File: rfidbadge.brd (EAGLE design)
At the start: 93.7 x 48.2 mm, 49 parts, among them Q1 BSS123, U1 ATMEGA328P_TQFP, U2 CLRC663, Y1 27.12 MHz

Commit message: Lots of layout
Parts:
- C10: device rcl:085CS_1AR -> SparkFun-Passives:EIA7343
- C28: value (none) -> 0.1 uF
- L1, L2, L3: device rcl:L0201 -> SparkFun-Passives:0603
- moved C26 16.8 mm to (54.9, 37.1)
- moved C28 15.5 mm to (52.1, 33.0), turned to 270 degrees
- moved R6 7.53 mm to (58.1, 37.1), turned to 180 degrees
- moved C16 6.67 mm to (35.6, 25.7)
- moved R4 6.24 mm to (60.0, 31.4)
- moved C27 5.83 mm to (55.6, 25.4), turned to 180 degrees
- moved C23 5.43 mm to (56.5, 27.9), turned to 270 degrees
- moved C5 5.41 mm to (48.6, 26.4), turned to 270 degrees
- moved R3 5.26 mm to (52.4, 27.6)
- moved R2 4.97 mm to (52.4, 29.8)
- moved Q1 4.93 mm to (36.8, 39.7), turned to 90 degrees
- moved C10 4.80 mm to (47.3, 45.1)
- moved R1 3.86 mm to (33.7, 40.6), turned to 90 degrees
- moved C21 2.69 mm to (56.5, 31.1), turned to 270 degrees
- moved L3 2.31 mm to (54.3, 32.4), turned to 180 degrees
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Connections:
- net GND: now also C10.C; no longer C10.-
- net VDD: now also C10.A; no longer C10.+
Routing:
- net GND: track 0.00 -> 23.2 mm
- net N$9: track 0.00 -> 15.0 mm
- net RXP: track 0.00 -> 10.9 mm, vias 0 -> 2
- net VDD: track 0.00 -> 10.7 mm
- net XTAL1: track 0.00 -> 7.74 mm
- net VMID: track 0.00 -> 7.73 mm
- net XTAL2: track 0.00 -> 7.31 mm
- net TVDD: track 0.00 -> 7.28 mm
- net N$1: track 0.00 -> 6.17 mm
- net N$2: track 0.00 -> 5.74 mm
- net TX1: track 0.00 -> 5.42 mm
- net C2-: track 0.00 -> 5.11 mm
- net C1-: track 0.00 -> 5.09 mm
- net N$6: track 0.00 -> 4.91 mm
- net TX2: track 0.00 -> 4.21 mm
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
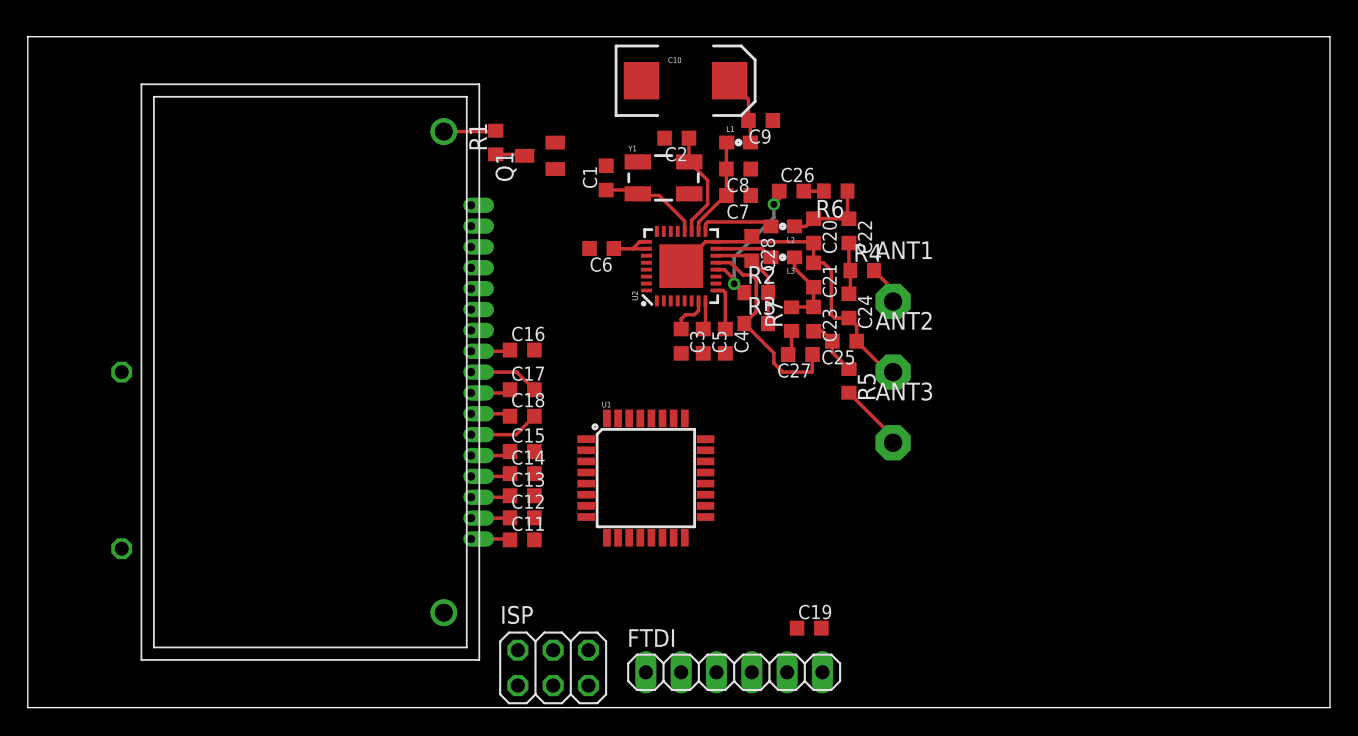
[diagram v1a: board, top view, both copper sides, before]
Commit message: Add antenna trace and ground planes
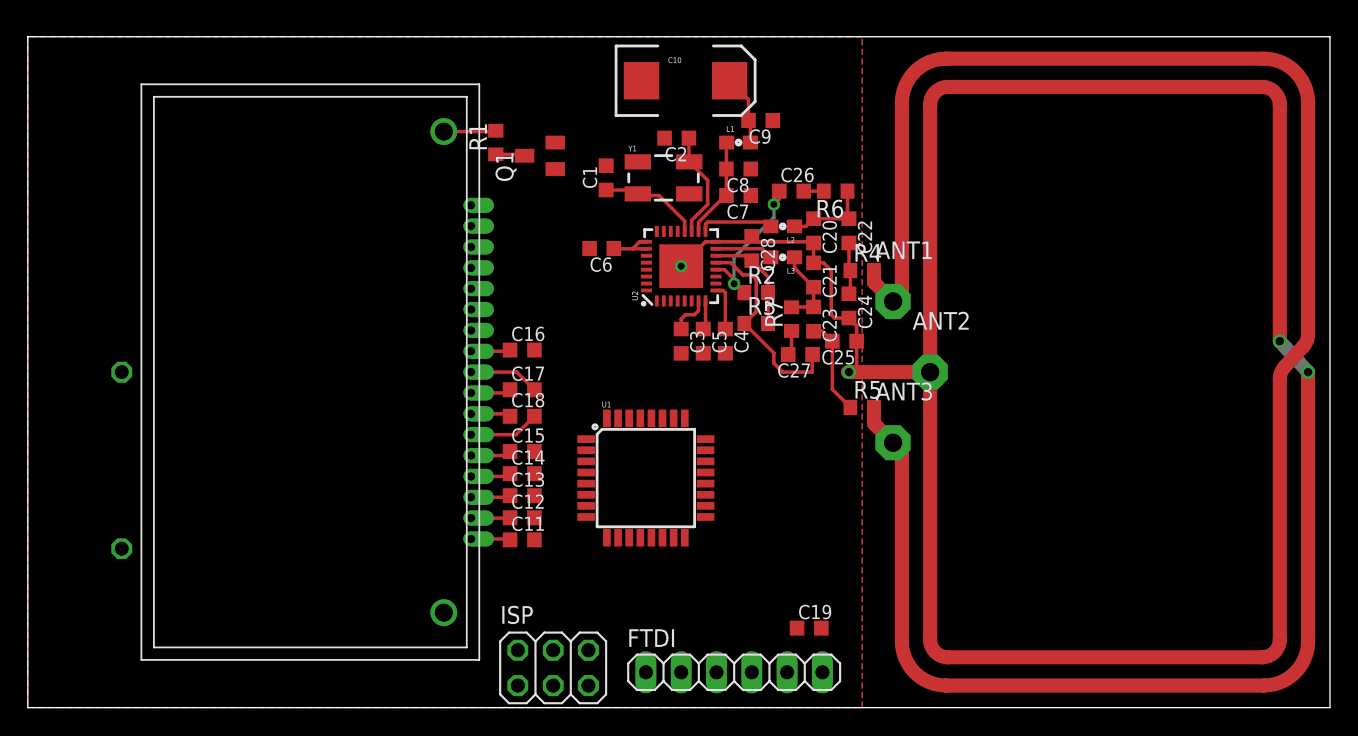
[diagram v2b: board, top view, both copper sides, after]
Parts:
- moved ANT2 2.67 mm to (64.9, 24.1)
- moved R5 2.13 mm to (60.0, 21.6), turned to 0 degrees
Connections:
- removed net N$5: ANT1.1, R4.2
- removed net N$6: ANT3.1, R5.2
- net GND: now also ANT1.1, ANT3.1, R4.2, R5.2
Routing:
- net GND: track 23.2 -> 297.3 mm, vias 0 -> 4
- net N$6: track 4.91 -> 0.00 mm
- net N$4: track 4.14 -> 6.94 mm
- net N$5: track 2.79 -> 0.00 mm
- added copper zone on layer 1, net GND
- added copper zone on layer 16, net GND
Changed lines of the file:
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@@
 <setting verticaltext="up"/>
 </settings>
-<grid distance="0.0125" unitdist="inch" unit="inch" style="lines" multiple="1" display="no" altdistance="0.025" altunitdist="inch" altunit="inch"/>
+<grid distance="0.0125" unitdist="inch" unit="inch" style="lines" multiple="1" display="yes" altdistance="0.025" altunitdist="inch" altunit="inch"/>
 <layers>
 <layer number="1" name="Top" color="4" fill="1" visible="yes" active="yes"/>
@@
 </element>
 <element name="R4" library="rcl" package="R0603" value="" x="60.0075" y="31.4325"/>
-<element name="R5" library="rcl" package="R0603" value="" x="59.055" y="23.495" rot="R270"/>
+<element name="R5" library="rcl" package="R0603" value="" x="60.0075" y="21.59"/>
 <element name="ANT1" library="discrete" package="PAD-01" value="" x="62.23" y="29.21"/>
-<element name="ANT2" library="discrete" package="PAD-01" value="" x="62.23" y="24.13"/>
+<element name="ANT2" library="discrete" package="PAD-01" value="" x="64.897" y="24.13"/>
 <element name="ANT3" library="discrete" package="PAD-01" value="" x="62.23" y="19.05"/>
 <element name="R6" library="rcl" package="R0603" value="" x="58.1025" y="37.1475" rot="R180"/>
@@
 <contactref element="FTDI" pad="2"/>
 <contactref element="U$1" pad="NEG"/>
-<wire x1="49.49" y1="33.5" x2="48.74" y2="33.5" width="0.254" layer="1"/>
-<wire x1="48.74" y1="33.5" x2="46.99" y2="31.75" width="0.254" layer="1"/>
 <wire x1="49.49" y1="33.5" x2="56.43" y2="33.5" width="0.254" layer="1"/>
 <wire x1="56.43" y1="33.5" x2="56.515" y2="33.415" width="0.254" layer="1"/>
@@
 <wire x1="59.6125" y1="26.3525" x2="59.6125" y2="27.46" width="0.254" layer="1"/>
 <wire x1="59.6125" y1="27.46" x2="59.055" y2="28.0175" width="0.254" layer="1"/>
-<wire x1="59.6125" y1="26.3525" x2="61.835" y2="24.13" width="0.254" layer="1"/>
-<wire x1="61.835" y1="24.13" x2="62.23" y2="24.13" width="0.254" layer="1"/>
-<wire x1="51.9925" y1="38.735" x2="53.58" y2="42.2275" width="0" layer="19" extent="1-1"/>
-<wire x1="51.9925" y1="36.83" x2="51.9925" y2="38.735" width="0" layer="19" extent="1-1"/>
-<wire x1="52.07" y1="33.895" x2="51.9925" y2="36.83" width="0" layer="19" extent="1-1"/>
-<wire x1="49.49" y1="33.5" x2="52.07" y2="33.895" width="0" layer="19" extent="1-1"/>
-<wire x1="46.99" y1="25.4775" x2="46.99" y2="31.75" width="0" layer="19" extent="1-1"/>
-<wire x1="48.5775" y1="25.4775" x2="46.99" y2="25.4775" width="0" layer="19" extent="1-1"/>
-<wire x1="50.165" y1="25.4775" x2="48.5775" y2="25.4775" width="0" layer="19" extent="1-1"/>
-<wire x1="45.7975" y1="40.9575" x2="51.9925" y2="38.735" width="0" layer="19" extent="1-1"/>
-<wire x1="44.1375" y1="45.085" x2="45.7975" y2="40.9575" width="0" layer="19" extent="1-1"/>
-<wire x1="41.5925" y1="38.975" x2="45.7975" y2="40.9575" width="0" layer="19" extent="1-1"/>
-<wire x1="37.93" y1="40.6375" x2="41.5925" y2="38.975" width="0" layer="19" extent="1-1"/>
-<wire x1="40.4" y1="33.02" x2="41.5925" y2="38.975" width="0" layer="19" extent="1-1"/>
-<wire x1="36.435" y1="25.7175" x2="40.4" y2="33.02" width="0" layer="19" extent="1-1"/>
-<wire x1="31.87" y1="27.13" x2="36.435" y2="25.7175" width="0" layer="19" extent="1-1"/>
-<wire x1="36.435" y1="18.415" x2="36.435" y2="25.7175" width="0" layer="19" extent="1-1"/>
-<wire x1="36.435" y1="16.8275" x2="36.435" y2="18.415" width="0" layer="19" extent="1-1"/>
-<wire x1="36.435" y1="15.24" x2="36.435" y2="16.8275" width="0" layer="19" extent="1-1"/>
-<wire x1="36.435" y1="13.6525" x2="36.435" y2="15.24" width="0" layer="19" extent="1-1"/>
-<wire x1="36.435" y1="12.065" x2="36.435" y2="13.6525" width="0" layer="19" extent="1-1"/>
-<wire x1="40.1574" y1="17.71" x2="36.435" y2="18.415" width="0" layer="19" extent="1-1"/>
-<wire x1="40.1574" y1="16.11" x2="40.1574" y2="17.71" width="0" layer="19" extent="1-1"/>
-<wire x1="48.7426" y1="16.91" x2="48.5775" y2="25.4775" width="0" layer="19" extent="1-1"/>
-<wire x1="40.3225" y1="4.1275" x2="36.435" y2="12.065" width="0" layer="19" extent="1-1"/>
-<wire x1="44.45" y1="2.54" x2="40.3225" y2="4.1275" width="0" layer="19" extent="1-1"/>
-<wire x1="46.99" y1="2.54" x2="44.45" y2="2.54" width="0" layer="19" extent="1-1"/>
-<wire x1="6.7564" y1="24.13" x2="31.87" y2="27.13" width="0" layer="19" extent="1-1"/>
+<wire x1="58.9775" y1="24.13" x2="59.3725" y2="24.13" width="1.016" layer="1"/>
+<wire x1="59.3725" y1="24.13" x2="64.897" y2="24.13" width="1.016" layer="1"/>
+<wire x1="64.897" y1="24.13" x2="64.897" y2="43.3705" width="1.016" layer="1"/>
+<wire x1="64.897" y1="43.3705" x2="66.167" y2="44.6405" width="1.016" layer="1" curve="-90"/>
+<wire x1="66.167" y1="44.6405" x2="88.773" y2="44.6405" width="1.016" layer="1"/>
+<wire x1="88.773" y1="44.6405" x2="90.043" y2="43.3705" width="1.016" layer="1" curve="-90"/>
+<wire x1="90.043" y1="43.3705" x2="90.043" y2="26.3525" width="1.016" layer="1"/>
+<wire x1="64.897" y1="24.13" x2="64.897" y2="4.8895" width="1.016" layer="1"/>
+<wire x1="64.897" y1="4.8895" x2="66.167" y2="3.6195" width="1.016" layer="1" curve="90"/>
+<wire x1="66.167" y1="3.6195" x2="88.773" y2="3.6195" width="1.016" layer="1"/>
+<wire x1="88.773" y1="3.6195" x2="90.043" y2="4.8895" width="1.016" layer="1" curve="90"/>
+<wire x1="91.742296875" y1="25.98860625" x2="90.375703125" y2="24.49389375" width="1.016" layer="1"/>
+<wire x1="90.375703125" y1="24.49389375" x2="90.043" y2="23.6369375" width="1.016" layer="1" curve="42.4362"/>
+<wire x1="90.043" y1="23.6369375" x2="90.043" y2="4.8895" width="1.016" layer="1"/>
+<wire x1="92.075" y1="43.4975" x2="92.075" y2="26.8455625" width="1.016" layer="1"/>
+<wire x1="92.075" y1="26.8455625" x2="91.742296875" y2="25.98860625" width="1.016" layer="1" curve="-42.4362"/>
+<wire x1="62.865" y1="29.21" x2="62.865" y2="43.4975" width="1.016" layer="1"/>
+<wire x1="62.865" y1="43.4975" x2="66.04" y2="46.6725" width="1.016" layer="1" curve="-90"/>
+<wire x1="66.04" y1="46.6725" x2="88.9" y2="46.6725" width="1.016" layer="1"/>
+<wire x1="88.9" y1="46.6725" x2="92.075" y2="43.4975" width="1.016" layer="1" curve="-90"/>
+<wire x1="62.23" y1="29.21" x2="62.865" y2="29.21" width="1.016" layer="1"/>
+<contactref element="R4" pad="2"/>
+<contactref element="ANT1" pad="1"/>
+<contactref element="R5" pad="2"/>
+<contactref element="ANT3" pad="1"/>
+<wire x1="92.075" y1="24.13" x2="92.075" y2="4.7625" width="1.016" layer="1"/>
+<wire x1="92.075" y1="4.7625" x2="88.9" y2="1.5875" width="1.016" layer="1" curve="-90"/>
+<wire x1="88.9" y1="1.5875" x2="66.04" y2="1.5875" width="1.016" layer="1"/>
+<wire x1="66.04" y1="1.5875" x2="62.865" y2="4.7625" width="1.016" layer="1" curve="-90"/>
+<wire x1="62.865" y1="4.7625" x2="62.865" y2="19.05" width="1.016" layer="1"/>
+<wire x1="62.23" y1="19.47" x2="62.23" y2="19.05" width="0.254" layer="1"/>
+<wire x1="62.865" y1="19.05" x2="62.23" y2="19.05" width="1.016" layer="1"/>
+<wire x1="90.043" y1="26.3525" x2="92.075" y2="24.13" width="1.016" layer="16"/>
+<via x="90.043" y="26.3525" extent="1-16" drill="0.6"/>
+<via x="92.075" y="24.13" extent="1-16" drill="0.6"/>
+<polygon width="0.254" layer="1">
+<vertex x="0" y="48.26"/>
+<vertex x="0" y="0"/>
+<vertex x="60.0075" y="0"/>
+<vertex x="60.0075" y="48.26"/>
+</polygon>
+<polygon width="0.254" layer="16">
+<vertex x="0" y="48.26"/>
+<vertex x="0" y="0"/>
+<vertex x="60.0075" y="0"/>
+<vertex x="60.0075" y="48.26"/>
+</polygon>
+<wire x1="59.6125" y1="26.3525" x2="59.6125" y2="24.37" width="0.254" layer="1"/>
+<wire x1="59.6125" y1="24.37" x2="59.3725" y2="24.13" width="0.254" layer="1"/>
+<via x="59.055" y="24.13" extent="1-16" drill="0.6"/>
+<wire x1="48.74" y1="33.5" x2="46.99" y2="31.75" width="0.254" layer="1"/>
+<via x="46.99" y="31.75" extent="1-16" drill="0.5"/>
+<wire x1="49.49" y1="33.5" x2="48.74" y2="33.5" width="0.254" layer="1"/>
+<wire x1="60.8575" y1="31.4325" x2="60.8575" y2="30.5825" width="1.016" layer="1"/>
+<wire x1="60.8575" y1="30.5825" x2="62.23" y2="29.21" width="1.016" layer="1"/>
+<wire x1="60.8575" y1="21.59" x2="60.8575" y2="20.4225" width="1.016" layer="1"/>
+<wire x1="60.8575" y1="20.4225" x2="62.23" y2="19.05" width="1.016" layer="1"/>
 </signal>
 <signal name="EXTCLK">
@@
 <wire x1="56.515" y1="27.065" x2="57.15" y2="27.065" width="0.254" layer="1"/>
 <wire x1="57.15" y1="27.065" x2="57.8625" y2="26.3525" width="0.254" layer="1"/>
-<wire x1="57.8625" y1="26.3525" x2="57.8625" y2="25.5375" width="0.254" layer="1"/>
-<wire x1="57.8625" y1="25.5375" x2="59.055" y2="24.345" width="0.254" layer="1"/>
-</signal>
-<signal name="N$5">
-<contactref element="R4" pad="2"/>
-<contactref element="ANT1" pad="1"/>
-<wire x1="60.8575" y1="31.4325" x2="62.23" y2="30.06" width="0.254" layer="1"/>
-<wire x1="62.23" y1="30.06" x2="62.23" y2="29.21" width="0.254" layer="1"/>
-</signal>
-<signal name="N$6">
-<contactref element="R5" pad="2"/>
-<contactref element="ANT3" pad="1"/>
-<wire x1="59.055" y1="22.645" x2="62.23" y2="19.47" width="0.254" layer="1"/>
-<wire x1="62.23" y1="19.47" x2="62.23" y2="19.05" width="0.254" layer="1"/>
+<wire x1="57.8625" y1="26.3525" x2="57.8625" y2="22.885" width="0.254" layer="1"/>
+<wire x1="57.8625" y1="22.885" x2="59.1575" y2="21.59" width="0.254" layer="1"/>
 </signal>
 <signal name="N$7">

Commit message: Finish routing
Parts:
- moved U1 1.00 mm to (45.4, 16.2), turned to 225 degrees
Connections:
- removed net VSS: FTDI.3, U2.27
- net GND: now also U2.27
- net VDD: now also FTDI.3
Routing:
- net VDD: track 10.7 -> 156.4 mm, vias 0 -> 2
- net RESET: track 0.00 -> 58.0 mm, vias 0 -> 3
- net SCK: track 0.00 -> 35.5 mm, vias 0 -> 2
- net SDA: track 0.00 -> 35.2 mm
- net MOSI: track 0.00 -> 34.2 mm
- net SCL: track 0.00 -> 33.6 mm
- net CS: track 0.00 -> 22.9 mm, vias 0 -> 2
- net LED: track 0.00 -> 21.7 mm
- net EXTCLK: track 0.00 -> 20.3 mm, vias 0 -> 2
- net MISO: track 0.00 -> 19.5 mm, vias 0 -> 2
- net A0: track 0.00 -> 19.0 mm
- net TXD: track 0.00 -> 14.0 mm, vias 0 -> 1
- net RXD: track 0.00 -> 12.6 mm, vias 0 -> 1
- net N$19: track 0.00 -> 3.21 mm
- net GND: track 297.3 -> 298.4 mm
